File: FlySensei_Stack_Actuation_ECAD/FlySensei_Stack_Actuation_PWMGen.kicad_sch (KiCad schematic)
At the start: 37 parts, among them U1 PCA9685BS

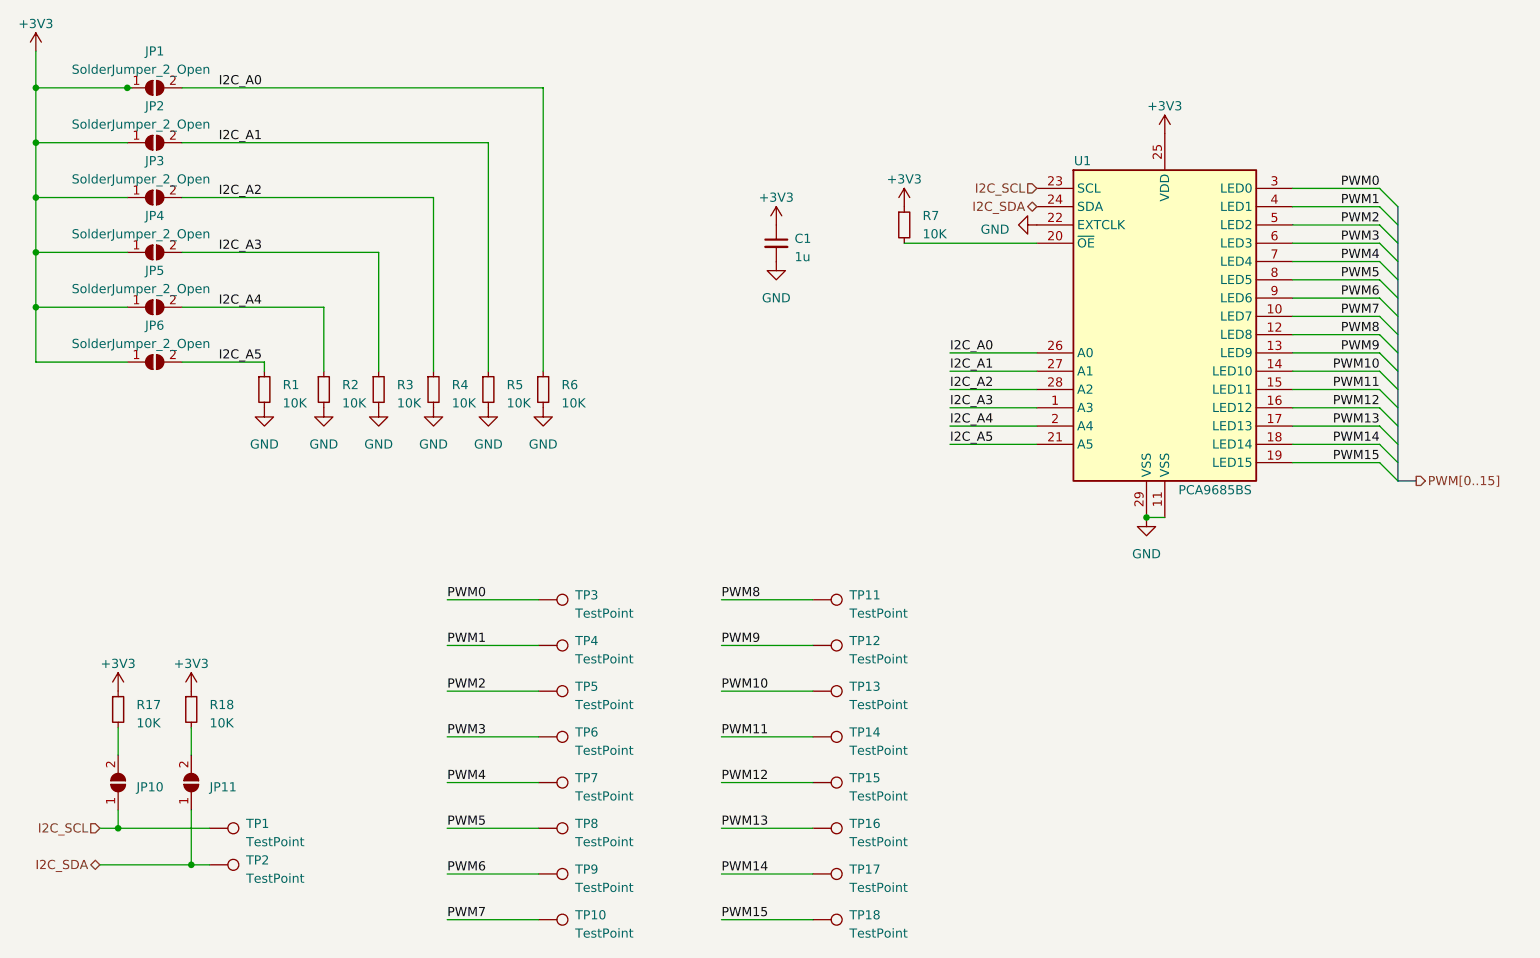
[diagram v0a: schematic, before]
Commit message: Change PWM generation IC package to TSSOP due to availibility
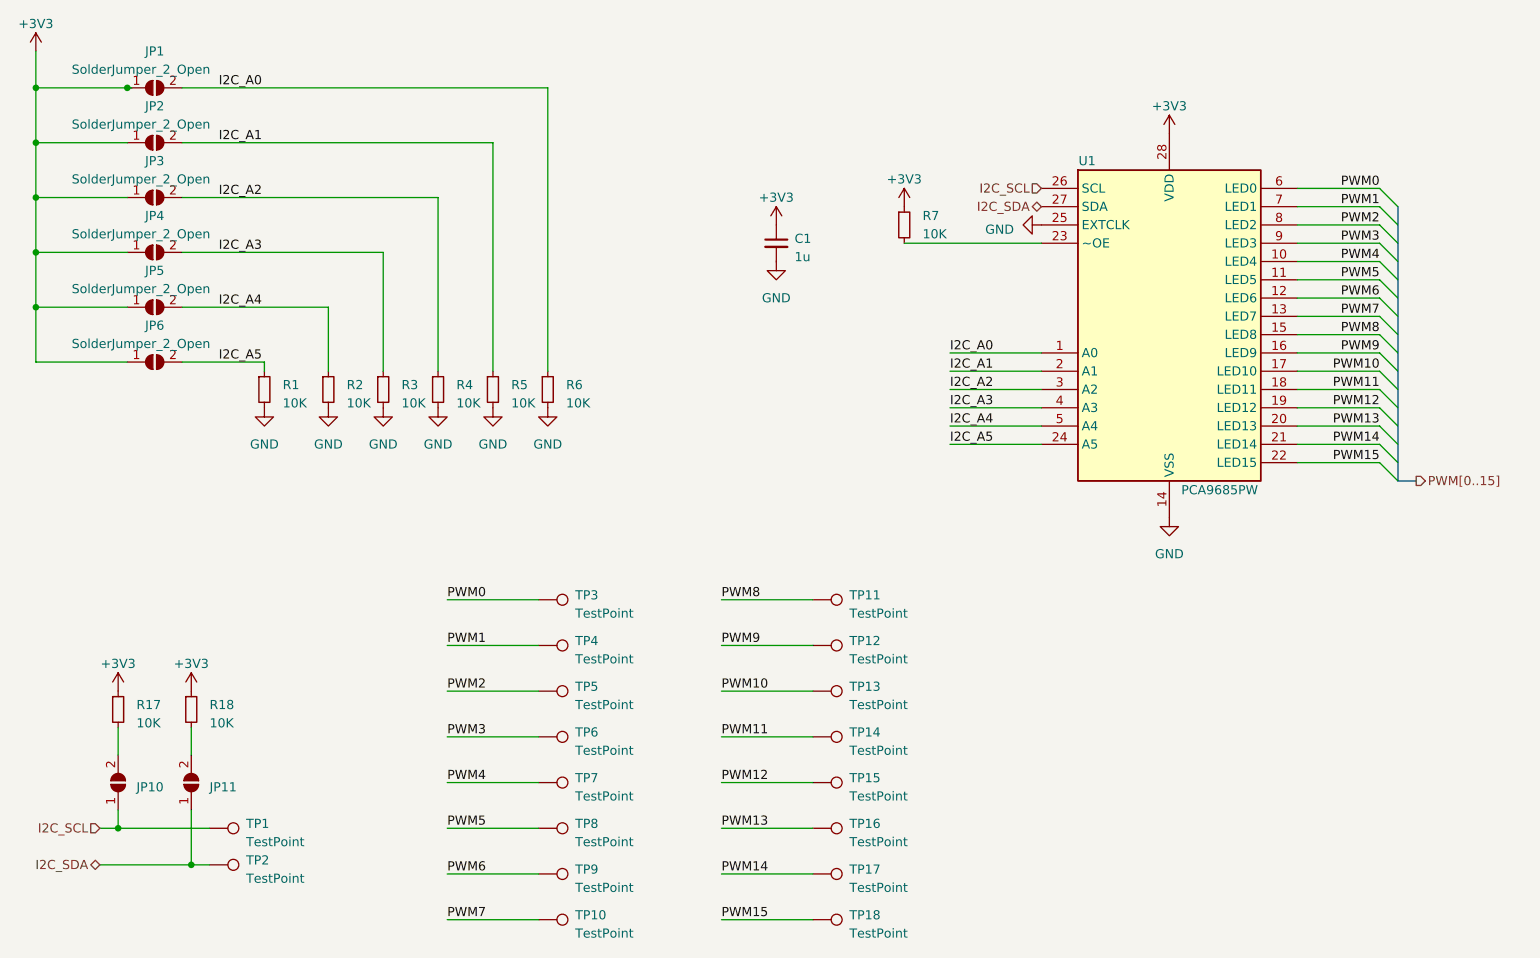
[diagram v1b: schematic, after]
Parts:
- U1: value PCA9685BS -> PCA9685PW; footprint Package_DFN_QFN:QFN-28-1EP_6x6mm_P0.65mm_EP4.25x4.25mm -> Package_SO:TSSOP-28_4.4x9.7mm_P0.65mm; symbol Driver_LED:PCA9685BS -> Driver_LED:PCA9685PW
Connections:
- net +3V3: now also U1.28 (VDD); no longer U1.25 (VDD)
- net GND: now also U1.14 (VSS), U1.25 (EXTCLK); no longer U1.11 (VSS), U1.22 (EXTCLK), U1.29 (VSS)
- net I2C_A0: now also U1.1 (A0); no longer U1.26 (A0)
- net I2C_A1: now also U1.2 (A1); no longer U1.27 (A1)
- net I2C_A2: now also U1.3 (A2); no longer U1.28 (A2)
- net I2C_A3: now also U1.4 (A3); no longer U1.1 (A3)
- net I2C_A4: now also U1.5 (A4); no longer U1.2 (A4)
- net I2C_A5: now also U1.24 (A5); no longer U1.21 (A5)
- net I2C_SCL: now also U1.26 (SCL); no longer U1.23 (SCL)
- net I2C_SDA: now also U1.27 (SDA); no longer U1.24 (SDA)
- net PWM0: now also U1.6 (LED0); no longer U1.3 (LED0)
- net PWM1: now also U1.7 (LED1); no longer U1.4 (LED1)
- net PWM10: now also U1.17 (LED10); no longer U1.14 (LED10)
- net PWM11: now also U1.18 (LED11); no longer U1.15 (LED11)
- net PWM12: now also U1.19 (LED12); no longer U1.16 (LED12)
- net PWM13: now also U1.20 (LED13); no longer U1.17 (LED13)
- net PWM14: now also U1.21 (LED14); no longer U1.18 (LED14)
- net PWM15: now also U1.22 (LED15); no longer U1.19 (LED15)
- net PWM2: now also U1.8 (LED2); no longer U1.5 (LED2)
- net PWM3: now also U1.9 (LED3); no longer U1.6 (LED3)
- net PWM4: now also U1.10 (LED4); no longer U1.7 (LED4)
- net PWM5: now also U1.11 (LED5); no longer U1.8 (LED5)
- net PWM6: now also U1.12 (LED6); no longer U1.9 (LED6)
- net PWM7: now also U1.13 (LED7); no longer U1.10 (LED7)
- net PWM8: now also U1.15 (LED8); no longer U1.12 (LED8)
- net PWM9: now also U1.16 (LED9); no longer U1.13 (LED9)
- net at R7.2: now also U1.23 (~OE); no longer U1.20 (~OE)
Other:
- moved on the sheet: R2, R3, R4, R5, R6
